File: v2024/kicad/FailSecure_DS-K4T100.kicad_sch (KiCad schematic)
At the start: 72 parts, among them CN1 WJ2EDGRC-5.08-2P, CN2 WJ2EDGRC-5.08-2P, CN3 WJ2EDGRC-5.08-8P, CN4 WAFER-200W-4A, CN5 WJ2EDGRC-5.08-2P, CN6 WAFER-200W-4A, CN7 WJ2EDGRC-5.08-2P, Q1 BSS138, Q2 BSS138, SW1 1TS002B-2300-4301, SW2 1TS002B-2300-4301, U1 PicoW, U2 TPS563200DDCR, U3 BX-DS2.54-4PTP, U4 SFH6206-3T

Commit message: Kicad, update schematic for access control v2025
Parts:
- removed CN4, CN6: WAFER-200W-4A, WAFER-200W-4A:CONN-SMD_4P-P2.00_HANBO_WAFER-200W-4A, symbol WAFER-200W-4A:WAFER-200W-4A
- removed CN7: WJ2EDGRC-5.08-2P, WJ2EDGRC-5.08-2P:CONN-TH_2P-P5.08_WJ2EDGRC-5.08-2P, symbol WJ2EDGRC-5.08-2P:WJ2EDGRC-5.08-2P
- removed D6: 1N4148W-TP, digikey-footprints:SOD-123, symbol dk_Diodes-Rectifiers-Single:1N4148W-TP
- added C17: 0.1u, Capacitor_SMD:C_0805_2012Metric, symbol SparkFun-Capacitor:C
- added C18, C19, C20: 1u, Capacitor_SMD:C_1206_3216Metric, symbol SparkFun-Capacitor:C
- added CN4: WAFER-200W-4P, WAFER-200W-4P:CONN-SMD_WAFER-200W-4P, symbol WAFER-200W-4P:WAFER-200W-4P
- added D6, D7: SMAJ26A, Diode_SMD:D_SMA, symbol Diode:SMAJ26A
- added Q3: BSS138, digikey-footprints:SOT-23-3, symbol dk_Transistors-FETs-MOSFETs-Single:BSS138
- added R27, R31: 0R, Resistor_SMD:R_0603_1608Metric, symbol Device:R
- added R28, R29: 10k, Resistor_SMD:R_0805_2012Metric, symbol Device:R
- added R30: 100R, Resistor_SMD:R_0805_2012Metric, symbol Device:R
- added U5, U6: HX PM2.54-2X5P WT, HX_PM2.54-2x5P_WT:HDR-SMD_10P-P2.54-H-F-R2-C5-W8.5, symbol HX_PM2.54-2x5P_WT:HXPM2.54-2X5PWT
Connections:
- net +3.3V: now also C20.1, CN4.2, R27.1, U6.10
- net +5V: now also C19.1, U5.1, U6.1
- net AIN_ADC2: now also U5.10
- net DI_ZeroCross: now also R31.1; no longer C16.2, R24.1, U4.4
- net DSK4T100_DoorStatus: now also C13.2, R13.1
- net DSK4T100_LockStatus: now also C14.2, R14.1
- net GND: now also C17.2, C18.2, C19.2, C20.2, CN4.1, CN4.5, CN4.6, D7.2 (A2), Q3.2 (S), R28.1, U5.5, U5.6, U6.5, U6.6
- net I2C0_SCL: now also CN4.4, U6.8
- net I2C0_SDA: now also CN4.3, U6.7
- net I2C1_SCL: now also U6.3
- net I2C1_SDA: now also U6.4
- net VIN: now also D6.1 (A1), R29.2
- net DO_GPIO0: now reaches U1.1 (GPIO0)
- net DO_GPIO0: now also U5.3
- net DO_GPIO1: now reaches U1.2 (GPIO1)
- net DO_GPIO1: now also U5.4
- net DI_DoorLock_LockStatus: now reaches U1.27 (GPIO21)
- net DI_DoorLock_LockStatus: now also R12.2
- net AIN_ADC0: now reaches U1.31 (GPIO26_ADC0)
- net AIN_ADC0: now also U5.8
- net AIN_ADC1: now reaches U1.32 (GPIO27_ADC1)
- net AIN_ADC1: now also U5.9
- net ADC_VREF: now reaches U1.35 (ADC_VREF)
- net ADC_VREF: now also C17.1, C18.1, R27.2
- net at Q2.3 (D), R7.1, Relay1.2: now also D6.2 (A2)
- net V_DSK4T100: now reaches CN3.1, Relay1.3
- net DSK4T100_Open: now reaches CN3.8
- net DSK4T100_Open: now also D7.1 (A1), Q3.3 (D), R29.1
- removed net DI_DoorStatus: C13.2, R11.2, R13.1, U1.25 (GPIO19)
- removed net DI_LockStatus: C14.2, R12.2, R14.1, U1.26 (GPIO20)
- net DO_DoorLock renamed DO_DoorLock_PWR
- new net: C16.2, R24.1, R31.2, U4.4
- new net: Q3.1 (G), R28.2, R30.1
- new net DI_DoorLock_DoorStatus: R11.2, U1.26 (GPIO20)
- new net DO_DoorLock_Open: R30.2, U1.25 (GPIO19)
- no-connect marks 16 -> 13
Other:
- note added: "BLACK -"
- note added: "BLUE NO"
- note added: "DIP Switch"
- note added: "GPIO RPi Pico (DO, ADC)"
- note added: "GREEN COM"
- note added: "Hikvision DSK4T100 Interface"
- note added: "I2C Ports"
- note added: "ORANGE OPEN"
- note added: "RED +"
- note added: "Reset button & Exit Button"
- note added: "Status LEDs"
- note added: "WHITE COM"
- note added: "WHITE NO"
- note added: "YELLOW NC"
- note added: "Zero-Crossing for Outage Detector"
- note removed: "BMS Interface"
- note removed: "Exit button"
- note removed: "Hikvision DSK4T100 DoorLock"
- note removed: "Status LEDs and RESET button"
- moved on the sheet: BUZZER1, C10, C11, C12, C13, C14, C16, C6, C8, C9, CN2, CN3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

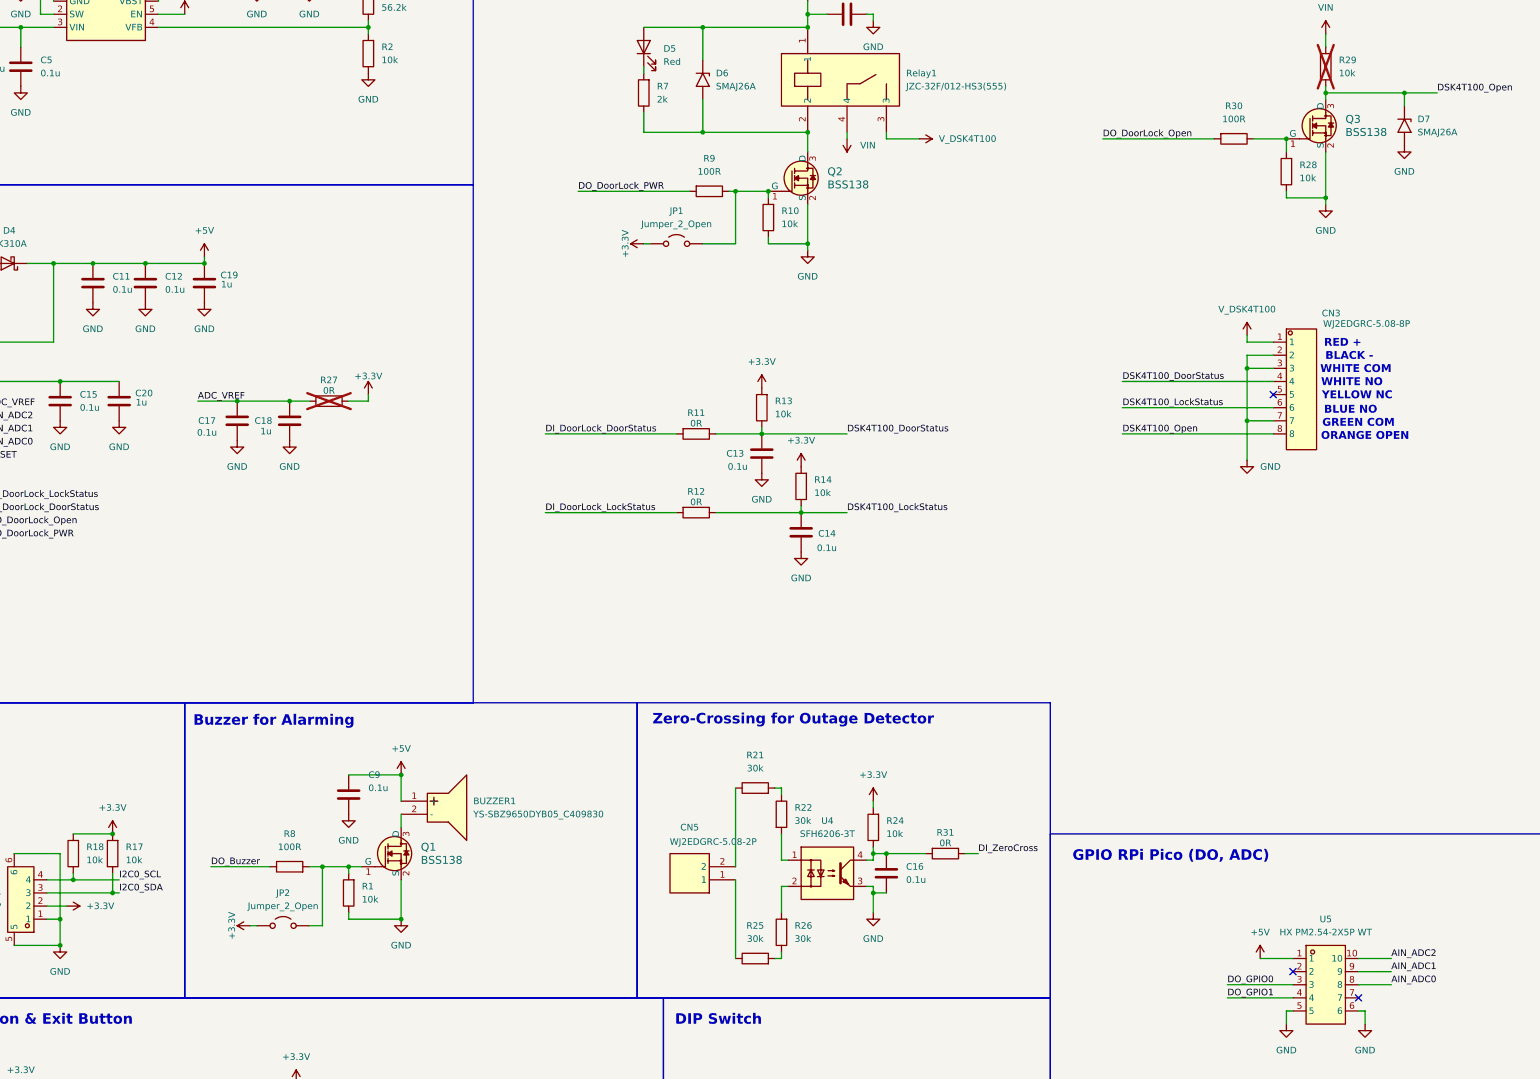
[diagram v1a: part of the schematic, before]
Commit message: Kicad, update PCB layout for a new schematic
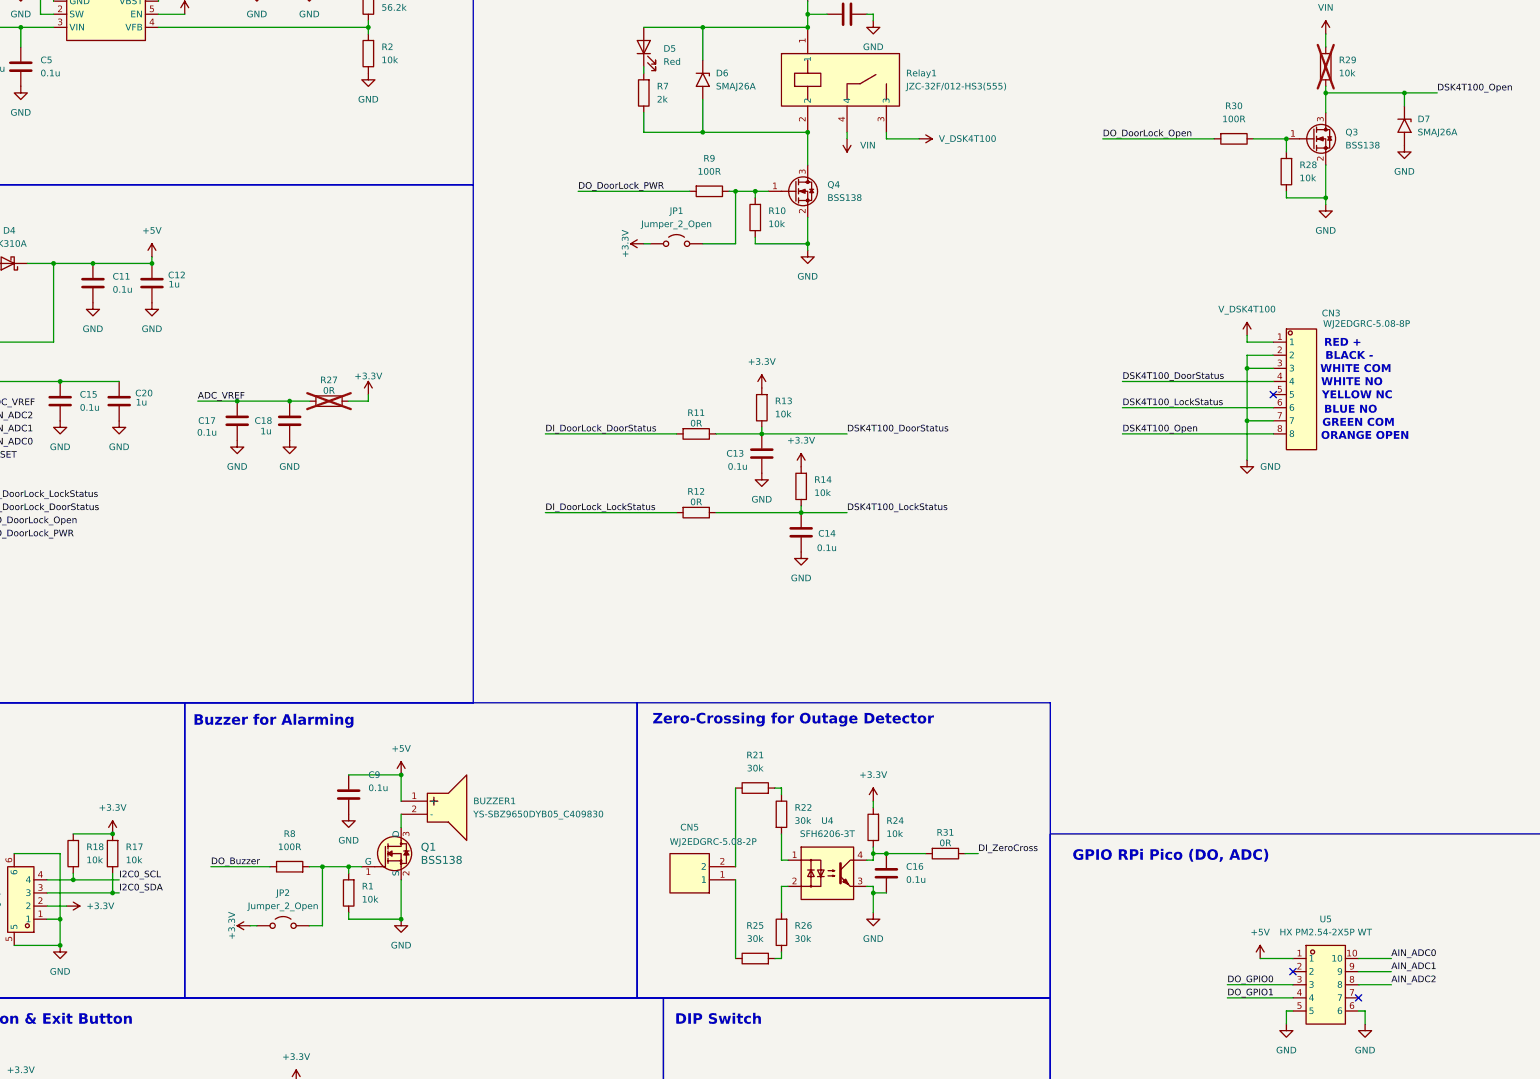
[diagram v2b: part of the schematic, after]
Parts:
- removed C12: 0.1u, Capacitor_SMD:C_0805_2012Metric, symbol SparkFun-Capacitor:C
- removed Q2, Q3: BSS138, digikey-footprints:SOT-23-3, symbol dk_Transistors-FETs-MOSFETs-Single:BSS138
- added Q3, Q4: BSS138, Package_TO_SOT_SMD:SOT-23-3, symbol Transistor_FET:BSS138
- renumbered C19 to C12
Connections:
- net AIN_ADC0: now also U5.10; no longer U5.8
- net AIN_ADC2: now also U5.8; no longer U5.10
- net DSK4T100_Open: now also Q3.3 (D)
- net GND: now also Q3.2 (S), Q4.2 (S)
- net at JP1.2 (B), R10.2, R9.1: now also Q4.1 (G)
- net at R28.2, R30.1: now also Q3.1 (G)
- net at D6.2 (A2), R7.1, Relay1.2: now also Q4.3 (D)
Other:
- moved on the sheet: C12, R10
